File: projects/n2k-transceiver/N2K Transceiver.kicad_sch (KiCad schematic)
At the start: 76 parts, among them J1 JTAG, SW1 SW_MEC_5G, SW2 SW_MEC_5G, SW3 SW_MEC_5G

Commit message: Standadized LEDs and GPIO resistors.
* Settled on 475 Ohm current limiting resistors for GPIO.
* Settled on Vishay TLMS1101-GS15 SMD LEDs.
* Added an LED to the Masthead controller for various status applications.

Signed-off-by: digimer <digital.mermaid@gmail.com>
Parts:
- removed LED2, LED3, LED4, LED5, LED6, LED7: LED, mr-stuff:ams OSRAM LS Q976.01, symbol Device:LED
- removed R21, R22, R23, R25, R26, R27, R28: 681R, mr-stuff:Stackpole RMCA0805, symbol Device:R
- added C64, C65: 0.1uF, mr-stuff:Kyocera AVX 0805, symbol mr-parts:Kyocera 08051C104K4Z2A
- added LED2, LED3, LED4, LED5, LED6, LED7: LED, mr-stuff:ams OSRAM LS Q976.01, symbol mr-parts:Vishay TLMS1101-GS15
- added R21, R22, R23, R25, R26, R27, R28, R52, R53: 475R, mr-stuff:Stackpole RNCP0805, symbol mr-parts:Stackpole RNCP0805FTD475R
- added R54: 10kR, mr-stuff:Stackpole RNCP0805, symbol mr-parts:Stackpole RNCP0805FTD10K0
- added SW4: SW_MEC_5G, mr-stuff:SW_TS03-66-50-BK-160-LCR-D-67, symbol Switch:SW_MEC_5G
- LED1: symbol Device:LED -> mr-parts:Vishay TLMS1101-GS15
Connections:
- net +3.3V: now also R54.1
- net GND: now also C64.2, C65.2, LED2.1 (K), LED3.1 (K), LED4.1 (K), LED5.1 (K), LED6.1 (K), LED7.1 (K); no longer SW3.3 (B), SW3.4 (B)
- net LED_ENABLE: now also R52.1; no longer R24.1, SW3.1 (A), SW3.2 (A)
- net N2K_RX_LED: now also R28.1
- net N2K_TX_LED: now also R27.1
- net POWER_LED: now also R21.1
- net SRV_UP_LED: now also R23.1
- net WIFI_RX_LED: now also R26.1
- net WIFI_TX_LED: now also R25.1
- net WIFI_UP_LED: now also R22.1
- net at LED1.2 (A): now also R21.2
- net CONFIG_SW: now reaches MCU1.20 (IO12)
- net CONFIG_SW: now also R53.1
- new net: LED2.2 (A), R22.2
- new net: LED7.2 (A), R28.2
- new net: R53.2, R54.2, SW4.1 (A), SW4.2 (A)
- new net: LED4.2 (A), R25.2
- new net: R24.1, R52.2, SW3.1 (A), SW3.2 (A)
- new net: LED6.2 (A), R27.2
- new net: C65.1, SW4.3 (B), SW4.4 (B)
- new net: LED3.2 (A), R23.2
- new net: C64.1, SW3.3 (B), SW3.4 (B)
- new net: LED5.2 (A), R26.2
- no-connect marks 13 -> 12
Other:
- note added: "Config"
- note added: "LEDs"
- company: The Digital Mermaid -> Tuskar Marine
- moved on the sheet: LED1

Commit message: Fixed Vishay TLMS1101-GS15 symbol.
Actually swapped the LEDs on the N2K transceiver.

Signed-off-by: digimer <digital.mermaid@gmail.com>
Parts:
- LED1, LED2, LED3, LED4, LED5, LED6, LED7: value LED -> TLMS1101-GS15; footprint mr-stuff:ams OSRAM LS Q976.01 -> mr-stuff:Vishay TLMS1101; Part ams OSRAM LS Q976.01-N1Q2-1 -> Vishay TLMS1101-GS15

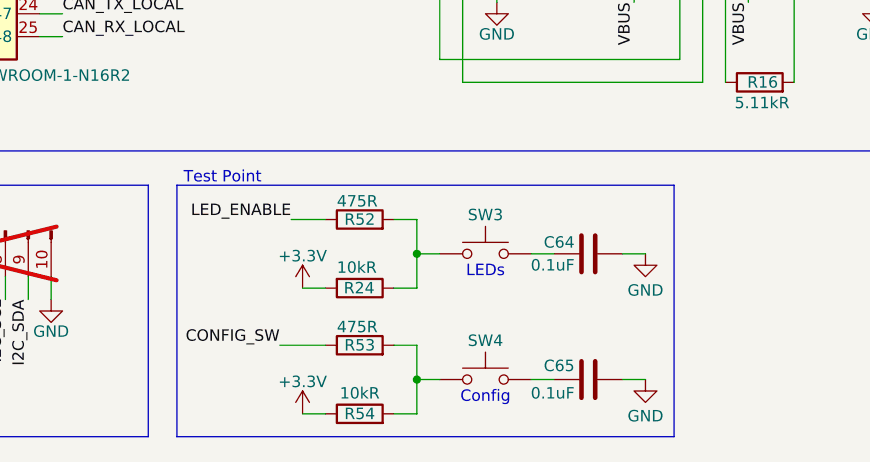
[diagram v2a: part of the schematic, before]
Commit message: Fixed debounce caps on the N2K Transceiver switches
Signed-off-by: digimer <digital.mermaid@gmail.com>
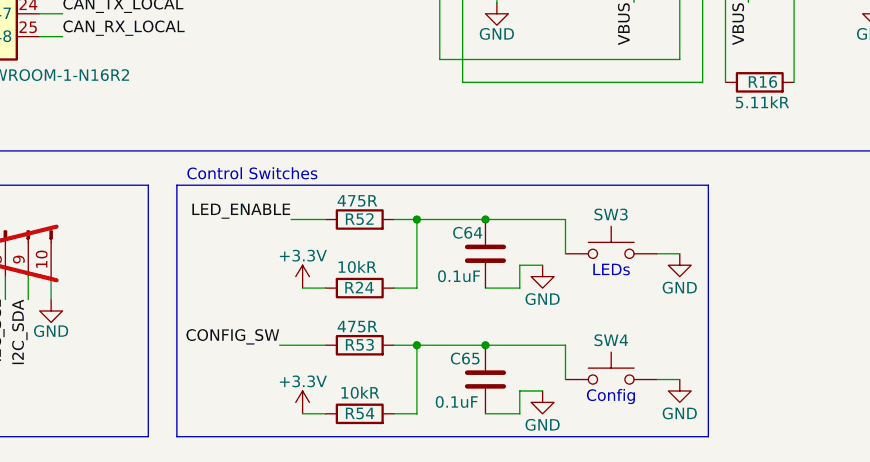
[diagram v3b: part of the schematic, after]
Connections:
- net GND: now also C64.1, C65.1, SW3.3 (B), SW3.4 (B), SW4.3 (B), SW4.4 (B); no longer C64.2, C65.2
- net at R53.2, R54.2, SW4.1 (A)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: now also C65.2
- net at R24.1, R52.2, SW3.1 (A)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: now also C64.2
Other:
- note added: "Control Switches"
- moved on the sheet: C64, C65, SW3, SW4

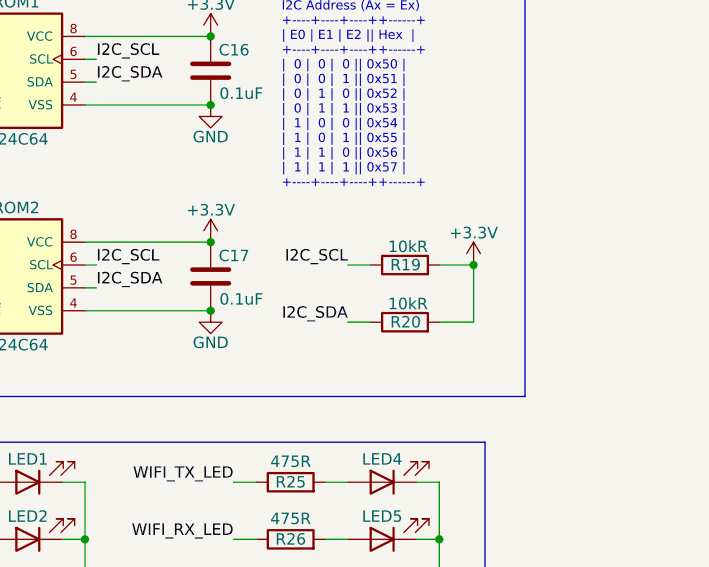
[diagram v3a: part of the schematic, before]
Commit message: Swapped the ROM on the MCTL to 128 KiB.
Swapped the I2C Pull-ups on the n2k-transceiver to 4.7kR.

Signed-off-by: digimer <digital.mermaid@gmail.com>
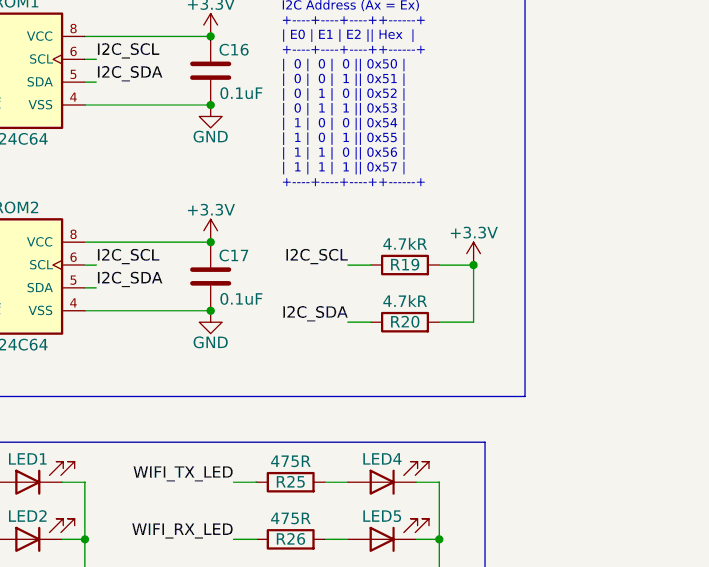
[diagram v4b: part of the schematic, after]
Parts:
- removed R19, R20: 10kR, mr-stuff:Stackpole_RNCP1206, symbol Device:R
- added R19, R20: 4.7kR, mr-stuff:Stackpole RMCA0805, symbol mr-parts:Stackpole RMCA0805FT4K70-HP
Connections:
- net +3.3V: now also R19.2, R20.2
- net I2C_SCL: now also R19.1
- net I2C_SDA: now also R20.1
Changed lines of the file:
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@@
 	)
 	(symbol
+		(lib_id "mr-parts:Stackpole RMCA0805FT4K70-HP")
+		(at 261.62 110.49 0)
+		(unit 1)
+		(body_style 1)
+		(exclude_from_sim no)
+		(in_bom yes)
+		(on_board yes)
+		(in_pos_files yes)
+		(dnp no)
+		(property "Reference" "R19"
+			(at 261.62 110.49 0)
+			(show_name no)
+			(do_not_autoplace no)
+			(effects
+				(font
+					(size 1.27 1.27)
+				)
+			)
+		)
+		(property "Value" "4.7kR"
+			(at 261.62 108.204 0)
+			(show_name no)
+			(do_not_autoplace no)
+			(effects
+				(font
+					(size 1.27 1.27)
+				)
+			)
+		)
+		(property "Footprint" "mr-stuff:Stackpole RMCA0805"
+			(at 261.62 119.888 0)
+			(hide yes)
+			(show_name no)
+			(do_not_autoplace no)
+			(effects
+				(font
+					(size 1.27 1.27)
+				)
+			)
+		)
+		(property "Datasheet" "https://www.seielect.com/catalog/SEI-RMCA.pdf"
+			(at 261.62 122.174 0)
+			(hide yes)
+			(show_name no)
+			(do_not_autoplace no)
+			(effects
+				(font
+					(size 1.27 1.27)
+				)
+			)
+		)
+		(property "Description" "4.7 kOhms ±1% 0.25W, 1/4W Chip Resistor 0805 (2012 Metric) Anti-Sulfur, Automotive AEC-Q200 Thick Film"
+			(at 261.62 117.602 0)
+			(hide yes)
+			(show_name no)
+			(do_not_autoplace no)
+			(effects
+				(font
+					(size 1.27 1.27)
+				)
+			)
+		)
+		(property "Part" "Stackpole RMCA0805FT4K70-HP"
+			(at 261.62 115.316 0)
+			(hide yes)
+			(show_name no)
+			(do_not_autoplace no)
+			(effects
+				(font
+					(size 1.27 1.27)
+				)
+			)
+		)
+		(pin "2"
+		)
+		(pin "1"
+		)
+		(instances
+			(project "N2K Transceiver"
+				(path "/2a070473-cb6e-4844-8f2a-5ea6a35ddb49"
+					(reference "R19")
+					(unit 1)
+				)
+			)
+		)
+	)
+	(symbol
 		(lib_id "Mechanical:MountingHole")
 		(at 19.05 180.34 0)
@@
 	)
 	(symbol
-		(lib_id "Device:R")
-		(at 261.62 116.84 90)
-		(unit 1)
-		(body_style 1)
-		(exclude_from_sim no)
-		(in_bom yes)
-		(on_board yes)
-		(in_pos_files yes)
-		(dnp no)
-		(property "Reference" "R20"
-			(at 263.398 116.84 90)
-			(show_name no)
-			(do_not_autoplace no)
-			(effects
-				(font
-					(size 1.27 1.27)
-				)
-				(justify left)
-			)
-		)
-		(property "Value" "10kR"
-			(at 264.16 114.808 90)
-			(show_name no)
-			(do_not_autoplace no)
-			(effects
-				(font
-					(size 1.27 1.27)
-				)
-				(justify left)
-			)
-		)
-		(property "Footprint" "mr-stuff:Stackpole_RNCP1206"
-			(at 261.62 118.618 90)
-			(hide yes)
-			(show_name no)
-			(do_not_autoplace no)
-			(effects
-				(font
-					(size 1.27 1.27)
-				)
-			)
-		)
-		(property "Datasheet" "https://www.seielect.com/catalog/SEI-RNCP.pdf"
-			(at 261.62 116.84 0)
-			(hide yes)
-			(show_name no)
-			(do_not_autoplace no)
-			(effects
-				(font
-					(size 1.27 1.27)
-				)
-			)
-		)
-		(property "Description" "10 kOhms ±1% 0.5W, 1/2W Chip Resistor 1206 (3216 Metric) Anti-Sulfur Thin Film"
-			(at 261.62 116.84 0)
-			(hide yes)
-			(show_name no)
-			(do_not_autoplace no)
-			(effects
-				(font
-					(size 1.27 1.27)
-				)
-			)
-		)
-		(property "Part" "Stackpole RNCP1206FTD10K0"
-			(at 261.62 116.84 90)
-			(hide yes)
-			(show_name no)
-			(do_not_autoplace no)
-			(effects
-				(font
-					(size 1.27 1.27)
-				)
-			)
-		)
-		(pin "2"
-		)
-		(pin "1"
-		)
-		(instances
-			(project "N2K Transceiver"
-				(path "/2a070473-cb6e-4844-8f2a-5ea6a35ddb49"
-					(reference "R20")
-					(unit 1)
-				)
-			)
-		)
-	)
-	(symbol
 		(lib_id "power:GND")
 		(at 240.03 92.71 0)
@@
 	)
 	(symbol
-		(lib_id "Device:R")
-		(at 261.62 110.49 90)
-		(unit 1)
-		(body_style 1)
-		(exclude_from_sim no)
-		(in_bom yes)
-		(on_board yes)
-		(in_pos_files yes)
-		(dnp no)
-		(property "Reference" "R19"
-			(at 263.398 110.49 90)
-			(show_name no)
-			(do_not_autoplace no)
-			(effects
-				(font
-					(size 1.27 1.27)
-				)
-				(justify left)
-			)
-		)
-		(property "Value" "10kR"
-			(at 264.16 108.458 90)
-			(show_name no)
-			(do_not_autoplace no)
-			(effects
-				(font
-					(size 1.27 1.27)
-				)
-				(justify left)
-			)
-		)
-		(property "Footprint" "mr-stuff:Stackpole_RNCP1206"
-			(at 261.62 112.268 90)
-			(hide yes)
-			(show_name no)
-			(do_not_autoplace no)
-			(effects
-				(font
-					(size 1.27 1.27)
-				)
-			)
-		)
-		(property "Datasheet" "https://www.seielect.com/catalog/SEI-RNCP.pdf"
-			(at 261.62 110.49 0)
-			(hide yes)
-			(show_name no)
-			(do_not_autoplace no)
-			(effects
-				(font
-					(size 1.27 1.27)
-				)
-			)
-		)
-		(property "Description" "10 kOhms ±1% 0.5W, 1/2W Chip Resistor 1206 (3216 Metric) Anti-Sulfur Thin Film"
-			(at 261.62 110.49 0)
-			(hide yes)
-			(show_name no)
-			(do_not_autoplace no)
-			(effects
-				(font
-					(size 1.27 1.27)
-				)
-			)
-		)
-		(property "Part" "Stackpole RNCP1206FTD10K0"
-			(at 261.62 110.49 90)
-			(hide yes)
-			(show_name no)
-			(do_not_autoplace no)
-			(effects
-				(font
-					(size 1.27 1.27)
-				)
-			)
-		)
-		(pin "2"
-		)
-		(pin "1"
-		)
-		(instances
-			(project "N2K Transceiver"
-				(path "/2a070473-cb6e-4844-8f2a-5ea6a35ddb49"
-					(reference "R19")
-					(unit 1)
-				)
-			)
-		)
-	)
-	(symbol
 		(lib_id "Switch:SW_MEC_5G")
 		(at 24.13 110.49 0)
@@
 					(unit 1)
 				)
+			)
+		)
+	)
+	(symbol
+		(lib_id "mr-parts:Stackpole RMCA0805FT4K70-HP")
+		(at 261.62 116.84 0)
+		(unit 1)
+		(body_style 1)
+		(exclude_from_sim no)
+		(in_bom yes)
+		(on_board yes)
+		(in_pos_files yes)
+		(dnp no)
+		(property "Reference" "R20"
+			(at 261.62 116.84 0)
+			(show_name no)
+			(do_not_autoplace no)
+			(effects
+				(font
+					(size 1.27 1.27)
+				)
+			)
+		)
+		(property "Value" "4.7kR"
+			(at 261.62 114.554 0)
+			(show_name no)
+			(do_not_autoplace no)
+			(effects
+				(font
+					(size 1.27 1.27)
+				)
+			)
+		)
+		(property "Footprint" "mr-stuff:Stackpole RMCA0805"
+			(at 261.62 126.238 0)
+			(hide yes)
+			(show_name no)
+			(do_not_autoplace no)
+			(effects
+				(font
+					(size 1.27 1.27)
+				)
+			)
+		)
+		(property "Datasheet" "https://www.seielect.com/catalog/SEI-RMCA.pdf"
+			(at 261.62 128.524 0)
+			(hide yes)
+			(show_name no)
+			(do_not_autoplace no)
+			(effects
+				(font
+					(size 1.27 1.27)
+				)
+			)
+		)
+		(property "Description" "4.7 kOhms ±1% 0.25W, 1/4W Chip Resistor 0805 (2012 Metric) Anti-Sulfur, Automotive AEC-Q200 Thick Film"
+			(at 261.62 123.952 0)
+			(hide yes)
+			(show_name no)
+			(do_not_autoplace no)
+			(effects
+				(font
+					(size 1.27 1.27)
+				)
+			)
+		)
+		(property "Part" "Stackpole RMCA0805FT4K70-HP"
+			(at 261.62 121.666 0)
+			(hide yes)
+			(show_name no)
+			(do_not_autoplace no)
+			(effects
+				(font
+					(size 1.27 1.27)
+				)
+			)
+		)
+		(pin "2"
+		)
+		(pin "1"
+		)
+		(instances
+			(project "N2K Transceiver"
+				(path "/2a070473-cb6e-4844-8f2a-5ea6a35ddb49"
+					(reference "R20")
+					(unit 1)
+				)
